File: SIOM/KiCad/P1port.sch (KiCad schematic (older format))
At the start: 14 parts, among them Q501 BSS138, U501 SC16IS740, Y501 7.3728MHz

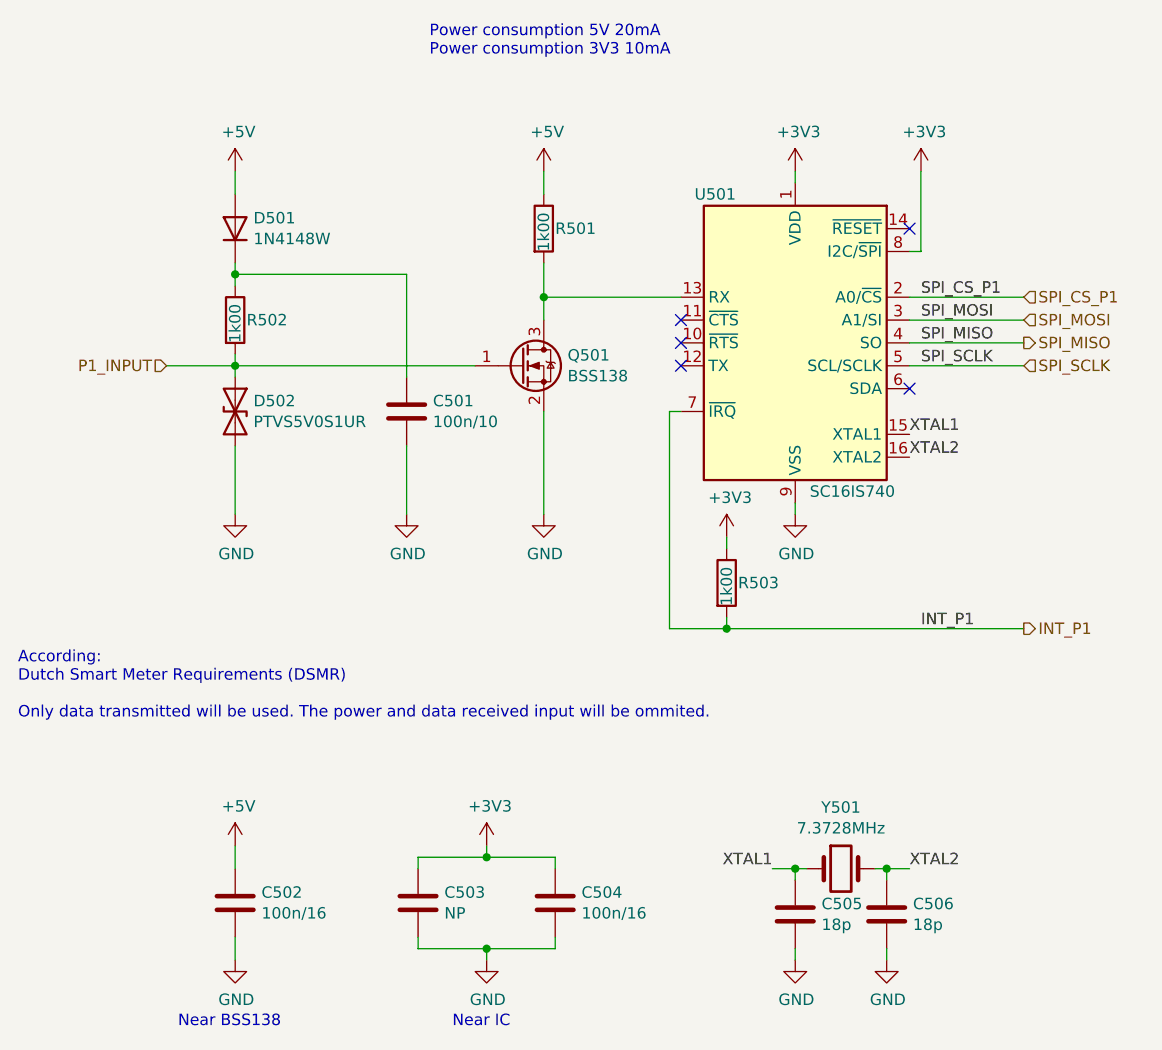
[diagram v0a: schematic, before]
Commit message: KiCad files SIOM_def
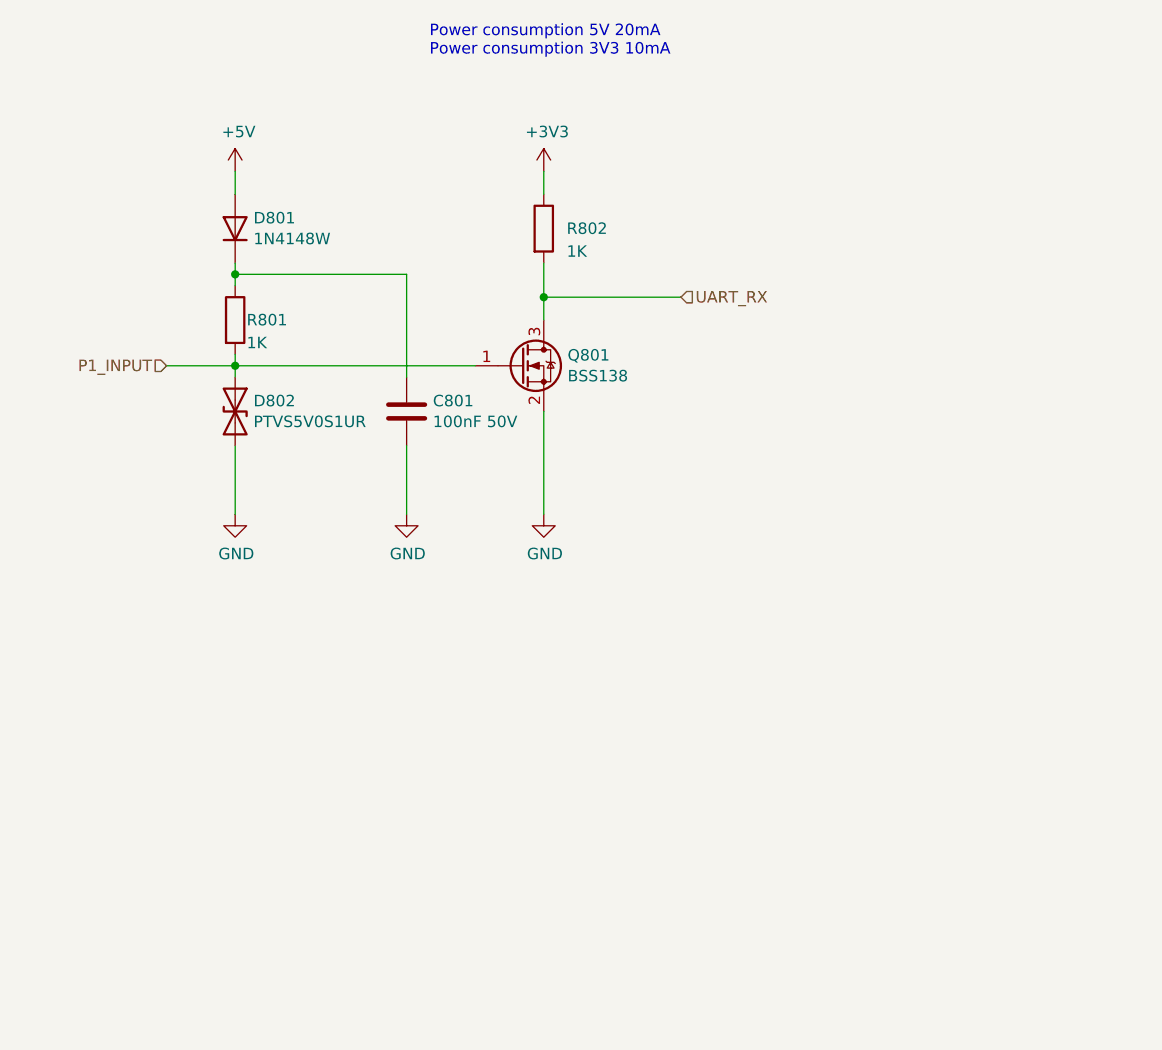
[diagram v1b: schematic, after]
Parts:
- removed C502, C504: 100n/16, Capacitor_SMD:C_0603_1608Metric, symbol SIOMv01-rescue:C-Device
- removed C503: NP, Capacitor_SMD:C_0805_2012Metric, symbol SIOMv01-rescue:C-Device
- removed C505, C506: 18p, Capacitor_SMD:C_0603_1608Metric, symbol SIOMv01-rescue:C-Device
- removed R503: 1k00, Resistor_SMD:R_0603_1608Metric, symbol SIOMv01-rescue:R-Device
- removed U501: SC16IS740, Package_SO:TSSOP-16_4.4x5mm_P0.65mm, symbol SIOMv01-rescue:SC16IS740-Interface_UART
- removed Y501: 7.3728MHz, Crystal:Crystal_SMD_3225-4Pin_3.2x2.5mm, symbol SIOMv01-rescue:Crystal-Device
- C801: renamed from C501; value 100n/10 -> 100nF 50V
- D802: renamed from D502; footprint Diode_SMD:Nexperia_CFP3_SOD-123W -> Diode_SMD:D_SOD-123
- R801: renamed from R502; value 1k00 -> 1K
- R802: renamed from R501; value 1k00 -> 1K
- renumbered D501 to D801, Q501 to Q801
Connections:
- net +3V3: now also R802.1
- net +5V: no longer R802.1
- net UART_RX: now reaches Q801.3 (D), R802.2
- no-connect marks 5 -> 0
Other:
- note removed: "According:\nDutch Smart Meter Requirements (DSMR)\n\nOnly data transmitted will be used. The power and data received input will be ommited."
- note removed: "Near BSS138"
- note removed: "Near IC"
